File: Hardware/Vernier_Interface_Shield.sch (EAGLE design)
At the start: 41 parts, among them U1 74HC4052SO, U2 LMV358

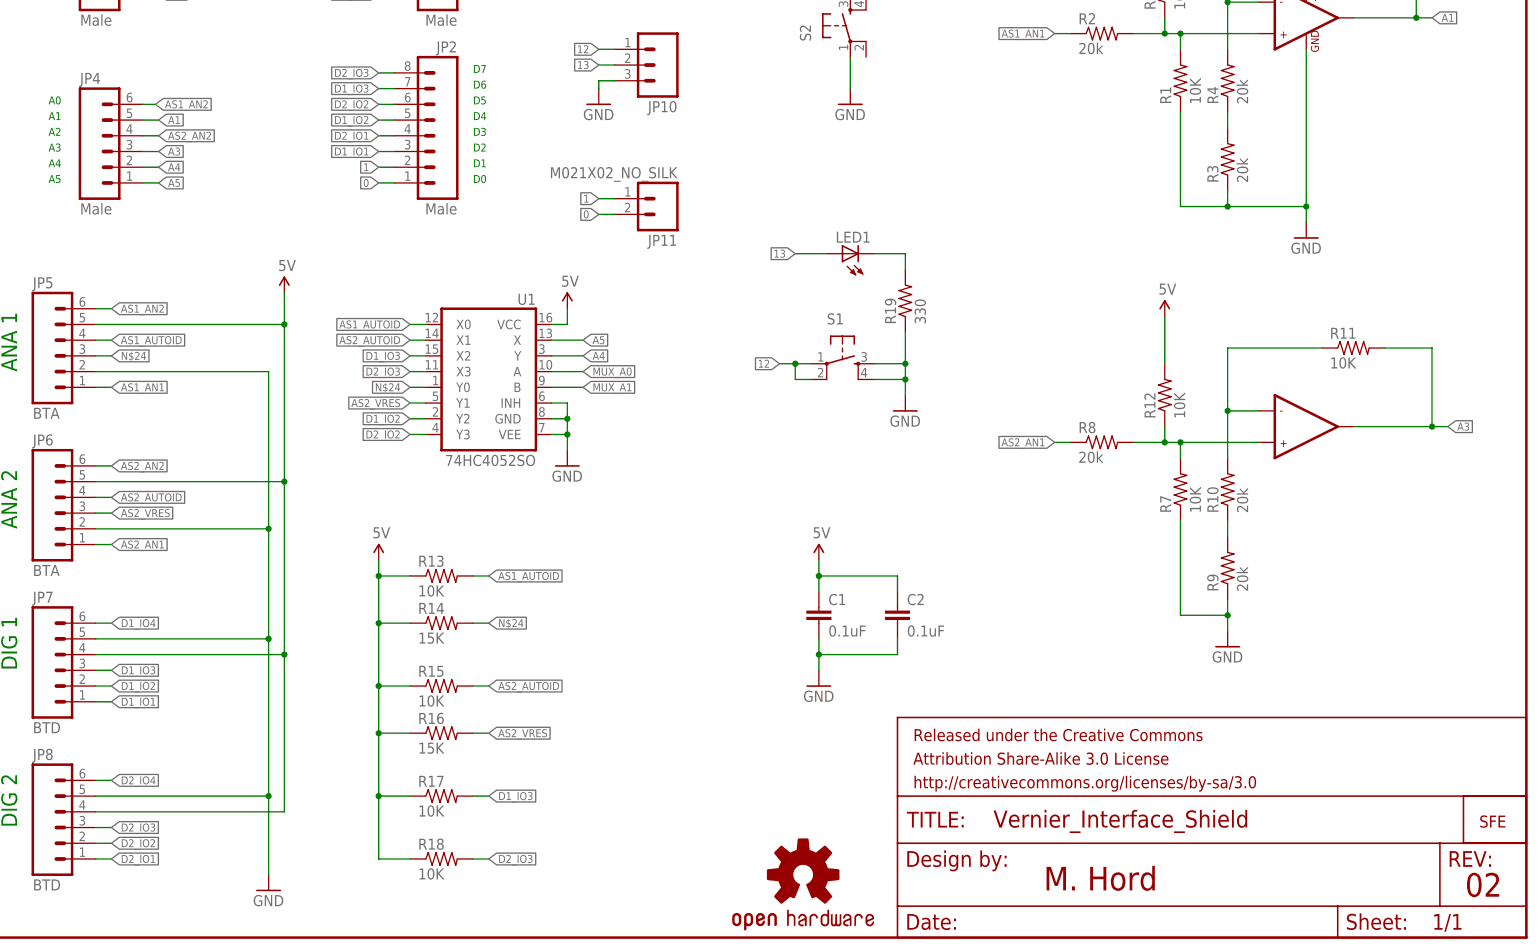
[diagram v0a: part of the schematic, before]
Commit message: Changed Pins 2 and 3 to BTD connector 1
Changed circuit so that Pins 2 and 3 are connected to BTD 1 - allows for
use of Hardware interrupts from Arduino.

Also cleaned up silks
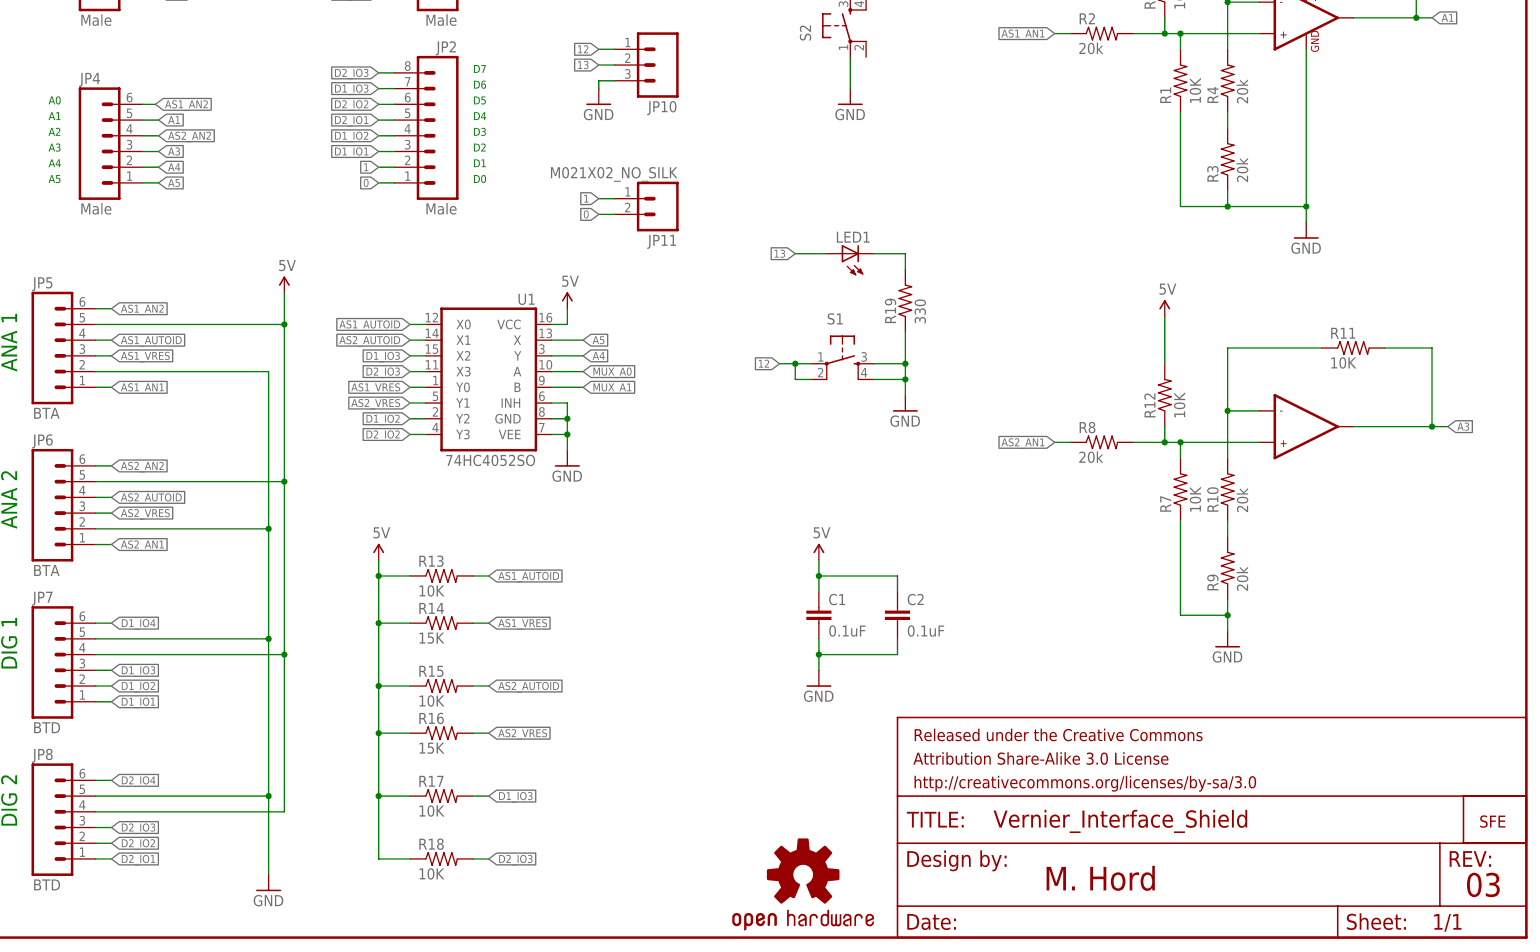
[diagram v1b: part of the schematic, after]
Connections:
- net N$24 renamed AS1_VRES
- net D1_IO2: now also JP2.4; no longer JP2.5
- net D2_IO1: now also JP2.5; no longer JP2.4
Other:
- note added: "03"
- note removed: "02"
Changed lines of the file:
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@@
 <text x="5.08" y="17.78" size="2.54" layer="91" rot="R90">DIG 2</text>
 <text x="170.942" y="7.62" size="3.81" layer="94">M. Hord</text>
-<text x="239.014" y="6.604" size="3.81" layer="94">02</text>
+<text x="239.014" y="6.604" size="3.81" layer="94">03</text>
 </plain>
 <instances>
@@
 </segment>
 </net>
-<net name="N$24" class="0">
-<segment>
-<wire x1="17.78" y1="93.98" x2="20.32" y2="93.98" width="0.1524" layer="91"/>
-<label x="20.32" y="93.98" size="1.27" layer="95" xref="yes"/>
-<pinref part="JP5" gate="G$1" pin="3"/>
-</segment>
-<segment>
-<pinref part="U1" gate="G$1" pin="Y0"/>
-<wire x1="71.12" y1="88.9" x2="68.58" y2="88.9" width="0.1524" layer="91"/>
-<label x="68.58" y="88.9" size="1.27" layer="95" rot="R180" xref="yes"/>
-</segment>
-<segment>
-<pinref part="R14" gate="G$1" pin="2"/>
-<wire x1="78.74" y1="50.8" x2="81.28" y2="50.8" width="0.1524" layer="91"/>
-<label x="81.28" y="50.8" size="1.27" layer="95" xref="yes"/>
-</segment>
-</net>
 <net name="AS1_AUTOID" class="0">
 <segment>
@@
 </segment>
 <segment>
+<pinref part="JP2" gate="G$1" pin="5"/>
+<wire x1="66.04" y1="132.08" x2="63.5" y2="132.08" width="0.1524" layer="91"/>
+<label x="63.5" y="132.08" size="1.27" layer="95" rot="R180" xref="yes"/>
+</segment>
+</net>
+<net name="D1_IO4" class="0">
+<segment>
+<wire x1="17.78" y1="50.8" x2="20.32" y2="50.8" width="0.1524" layer="91"/>
+<label x="20.32" y="50.8" size="1.27" layer="95" xref="yes"/>
+<pinref part="JP7" gate="G$1" pin="6"/>
+</segment>
+<segment>
+<pinref part="JP1" gate="G$1" pin="1"/>
+<wire x1="66.04" y1="152.4" x2="63.5" y2="152.4" width="0.1524" layer="91"/>
+<label x="63.5" y="152.4" size="1.27" layer="95" rot="R180" xref="yes"/>
+</segment>
+</net>
+<net name="D1_IO3" class="0">
+<segment>
+<wire x1="17.78" y1="43.18" x2="20.32" y2="43.18" width="0.1524" layer="91"/>
+<label x="20.32" y="43.18" size="1.27" layer="95" xref="yes"/>
+<pinref part="JP7" gate="G$1" pin="3"/>
+</segment>
+<segment>
+<pinref part="U1" gate="G$1" pin="X2"/>
+<wire x1="71.12" y1="93.98" x2="68.58" y2="93.98" width="0.1524" layer="91"/>
+<label x="68.58" y="93.98" size="1.27" layer="95" rot="R180" xref="yes"/>
+</segment>
+<segment>
+<pinref part="R17" gate="G$1" pin="2"/>
+<wire x1="78.74" y1="22.86" x2="81.28" y2="22.86" width="0.1524" layer="91"/>
+<label x="81.28" y="22.86" size="1.27" layer="95" xref="yes"/>
+</segment>
+<segment>
+<pinref part="JP2" gate="G$1" pin="7"/>
+<wire x1="66.04" y1="137.16" x2="63.5" y2="137.16" width="0.1524" layer="91"/>
+<label x="63.5" y="137.16" size="1.27" layer="95" rot="R180" xref="yes"/>
+</segment>
+</net>
+<net name="D1_IO2" class="0">
+<segment>
+<wire x1="17.78" y1="40.64" x2="20.32" y2="40.64" width="0.1524" layer="91"/>
+<label x="20.32" y="40.64" size="1.27" layer="95" xref="yes"/>
+<pinref part="JP7" gate="G$1" pin="2"/>
+</segment>
+<segment>
+<pinref part="U1" gate="G$1" pin="Y2"/>
+<wire x1="71.12" y1="83.82" x2="68.58" y2="83.82" width="0.1524" layer="91"/>
+<label x="68.58" y="83.82" size="1.27" layer="95" rot="R180" xref="yes"/>
+</segment>
+<segment>
 <pinref part="JP2" gate="G$1" pin="4"/>
 <wire x1="66.04" y1="129.54" x2="63.5" y2="129.54" width="0.1524" layer="91"/>
 <label x="63.5" y="129.54" size="1.27" layer="95" rot="R180" xref="yes"/>
-</segment>
-</net>
-<net name="D1_IO4" class="0">
-<segment>
-<wire x1="17.78" y1="50.8" x2="20.32" y2="50.8" width="0.1524" layer="91"/>
-<label x="20.32" y="50.8" size="1.27" layer="95" xref="yes"/>
-<pinref part="JP7" gate="G$1" pin="6"/>
-</segment>
-<segment>
-<pinref part="JP1" gate="G$1" pin="1"/>
-<wire x1="66.04" y1="152.4" x2="63.5" y2="152.4" width="0.1524" layer="91"/>
-<label x="63.5" y="152.4" size="1.27" layer="95" rot="R180" xref="yes"/>
-</segment>
-</net>
-<net name="D1_IO3" class="0">
-<segment>
-<wire x1="17.78" y1="43.18" x2="20.32" y2="43.18" width="0.1524" layer="91"/>
-<label x="20.32" y="43.18" size="1.27" layer="95" xref="yes"/>
-<pinref part="JP7" gate="G$1" pin="3"/>
-</segment>
-<segment>
-<pinref part="U1" gate="G$1" pin="X2"/>
-<wire x1="71.12" y1="93.98" x2="68.58" y2="93.98" width="0.1524" layer="91"/>
-<label x="68.58" y="93.98" size="1.27" layer="95" rot="R180" xref="yes"/>
-</segment>
-<segment>
-<pinref part="R17" gate="G$1" pin="2"/>
-<wire x1="78.74" y1="22.86" x2="81.28" y2="22.86" width="0.1524" layer="91"/>
-<label x="81.28" y="22.86" size="1.27" layer="95" xref="yes"/>
-</segment>
-<segment>
-<pinref part="JP2" gate="G$1" pin="7"/>
-<wire x1="66.04" y1="137.16" x2="63.5" y2="137.16" width="0.1524" layer="91"/>
-<label x="63.5" y="137.16" size="1.27" layer="95" rot="R180" xref="yes"/>
-</segment>
-</net>
-<net name="D1_IO2" class="0">
-<segment>
-<wire x1="17.78" y1="40.64" x2="20.32" y2="40.64" width="0.1524" layer="91"/>
-<label x="20.32" y="40.64" size="1.27" layer="95" xref="yes"/>
-<pinref part="JP7" gate="G$1" pin="2"/>
-</segment>
-<segment>
-<pinref part="U1" gate="G$1" pin="Y2"/>
-<wire x1="71.12" y1="83.82" x2="68.58" y2="83.82" width="0.1524" layer="91"/>
-<label x="68.58" y="83.82" size="1.27" layer="95" rot="R180" xref="yes"/>
-</segment>
-<segment>
-<pinref part="JP2" gate="G$1" pin="5"/>
-<wire x1="66.04" y1="132.08" x2="63.5" y2="132.08" width="0.1524" layer="91"/>
-<label x="63.5" y="132.08" size="1.27" layer="95" rot="R180" xref="yes"/>
 </segment>
 </net>
@@
 </segment>
 </net>
+<net name="AS1_VRES" class="0">
+<segment>
+<pinref part="U1" gate="G$1" pin="Y0"/>
+<wire x1="71.12" y1="88.9" x2="68.58" y2="88.9" width="0.1524" layer="91"/>
+<label x="68.58" y="88.9" size="1.27" layer="95" rot="R180" xref="yes"/>
+</segment>
+<segment>
+<wire x1="17.78" y1="93.98" x2="20.32" y2="93.98" width="0.1524" layer="91"/>
+<label x="20.32" y="93.98" size="1.27" layer="95" xref="yes"/>
+<pinref part="JP5" gate="G$1" pin="3"/>
+</segment>
+<segment>
+<pinref part="R14" gate="G$1" pin="2"/>
+<wire x1="78.74" y1="50.8" x2="81.28" y2="50.8" width="0.1524" layer="91"/>
+<label x="81.28" y="50.8" size="1.27" layer="95" xref="yes"/>
+</segment>
+</net>

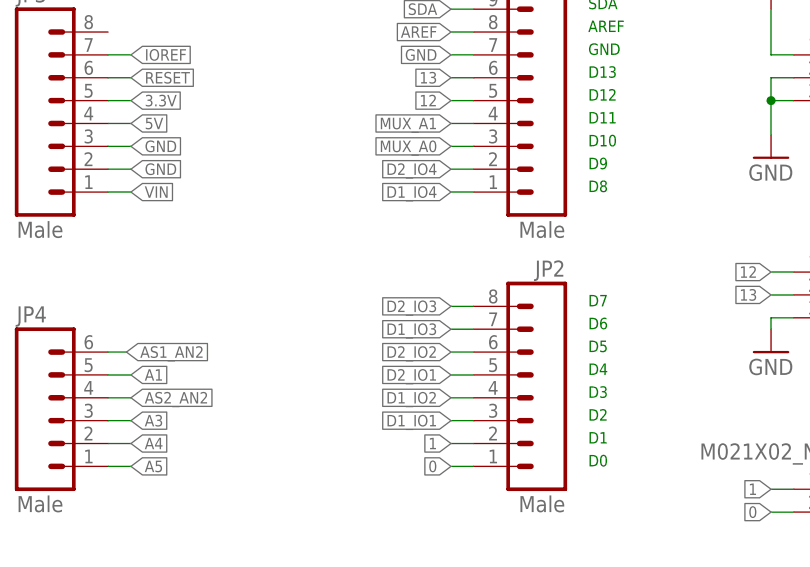
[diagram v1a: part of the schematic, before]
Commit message: Changed pins one last time...
Changed Digital Pins so that it's pins 2, 3, 4, 5 on Dig 1 and 6, 7, 8
,9 on Dig 2
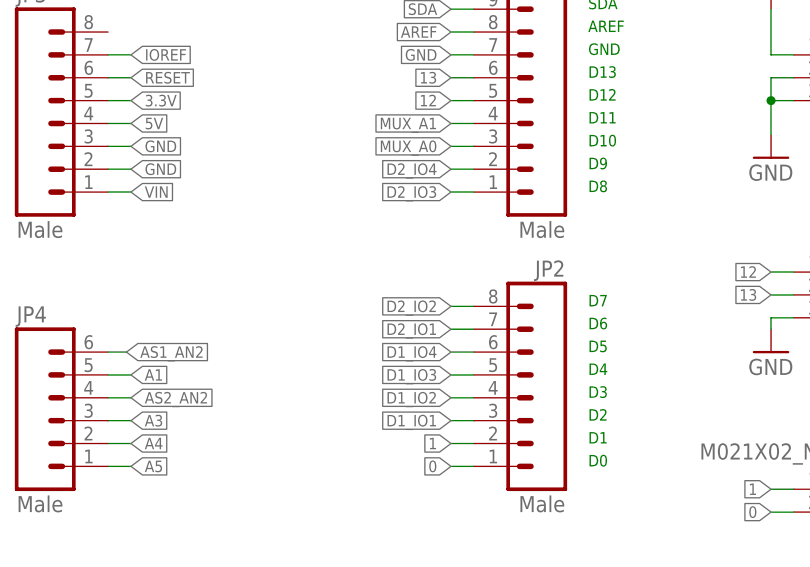
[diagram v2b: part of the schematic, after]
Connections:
- net D1_IO3: now also JP2.5; no longer JP2.7
- net D1_IO4: now also JP2.6; no longer JP1.1
- net D2_IO1: now also JP2.7; no longer JP2.5
- net D2_IO2: now also JP2.8; no longer JP2.6
- net D2_IO3: now also JP1.1; no longer JP2.8
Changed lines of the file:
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@@
 </segment>
 <segment>
-<pinref part="JP2" gate="G$1" pin="8"/>
-<wire x1="66.04" y1="139.7" x2="63.5" y2="139.7" width="0.1524" layer="91"/>
-<label x="63.5" y="139.7" size="1.27" layer="95" rot="R180" xref="yes"/>
+<pinref part="JP1" gate="G$1" pin="1"/>
+<wire x1="66.04" y1="152.4" x2="63.5" y2="152.4" width="0.1524" layer="91"/>
+<label x="63.5" y="152.4" size="1.27" layer="95" rot="R180" xref="yes"/>
 </segment>
 </net>
@@
 </segment>
 <segment>
-<pinref part="JP2" gate="G$1" pin="6"/>
-<wire x1="66.04" y1="134.62" x2="63.5" y2="134.62" width="0.1524" layer="91"/>
-<label x="63.5" y="134.62" size="1.27" layer="95" rot="R180" xref="yes"/>
+<pinref part="JP2" gate="G$1" pin="8"/>
+<wire x1="66.04" y1="139.7" x2="63.5" y2="139.7" width="0.1524" layer="91"/>
+<label x="63.5" y="139.7" size="1.27" layer="95" rot="R180" xref="yes"/>
 </segment>
 </net>
@@
 </segment>
 <segment>
-<pinref part="JP2" gate="G$1" pin="5"/>
-<wire x1="66.04" y1="132.08" x2="63.5" y2="132.08" width="0.1524" layer="91"/>
-<label x="63.5" y="132.08" size="1.27" layer="95" rot="R180" xref="yes"/>
+<pinref part="JP2" gate="G$1" pin="7"/>
+<wire x1="66.04" y1="137.16" x2="63.5" y2="137.16" width="0.1524" layer="91"/>
+<label x="63.5" y="137.16" size="1.27" layer="95" rot="R180" xref="yes"/>
 </segment>
 </net>
@@
 </segment>
 <segment>
-<pinref part="JP1" gate="G$1" pin="1"/>
-<wire x1="66.04" y1="152.4" x2="63.5" y2="152.4" width="0.1524" layer="91"/>
-<label x="63.5" y="152.4" size="1.27" layer="95" rot="R180" xref="yes"/>
+<pinref part="JP2" gate="G$1" pin="6"/>
+<wire x1="66.04" y1="134.62" x2="63.5" y2="134.62" width="0.1524" layer="91"/>
+<label x="63.5" y="134.62" size="1.27" layer="95" rot="R180" xref="yes"/>
 </segment>
 </net>
@@
 </segment>
 <segment>
-<pinref part="JP2" gate="G$1" pin="7"/>
-<wire x1="66.04" y1="137.16" x2="63.5" y2="137.16" width="0.1524" layer="91"/>
-<label x="63.5" y="137.16" size="1.27" layer="95" rot="R180" xref="yes"/>
+<pinref part="JP2" gate="G$1" pin="5"/>
+<wire x1="66.04" y1="132.08" x2="63.5" y2="132.08" width="0.1524" layer="91"/>
+<label x="63.5" y="132.08" size="1.27" layer="95" rot="R180" xref="yes"/>
 </segment>
 </net>
